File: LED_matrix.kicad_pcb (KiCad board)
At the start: 2 copper layers, 42 x 52 mm, 153 parts, among them J1 Conn_02x20_Odd_Even

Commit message: move to 0.2/0.5 vias
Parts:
- R17, R18, R19, R20, R21, R22, R23, R24, R25, R26, R27, R28, R29, R30, R31, R32: footprint Resistors_SMD:R_0603 -> Resistor_SMD:R_0603_1608Metric
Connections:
- J1 pad 1: Net-(J1-Pad1) -> (no net)
- J1 pad 10: Net-(J1-Pad10) -> (no net)
- J1 pad 11: Net-(J1-Pad11) -> (no net)
- J1 pad 12: Net-(J1-Pad12) -> (no net)
- J1 pad 13: Net-(J1-Pad13) -> (no net)
- J1 pad 14: Net-(J1-Pad14) -> (no net)
- J1 pad 17: Net-(J1-Pad17) -> (no net)
- J1 pad 2: Net-(J1-Pad2) -> (no net)
- J1 pad 20: Net-(J1-Pad20) -> (no net)
- J1 pad 24: Net-(J1-Pad24) -> (no net)
- J1 pad 25: Net-(J1-Pad25) -> (no net)
- J1 pad 26: Net-(J1-Pad26) -> (no net)
- J1 pad 27: Net-(J1-Pad27) -> (no net)
- J1 pad 28: Net-(J1-Pad28) -> (no net)
- J1 pad 3: Net-(J1-Pad3) -> (no net)
- J1 pad 30: Net-(J1-Pad30) -> (no net)
- J1 pad 34: Net-(J1-Pad34) -> (no net)
- J1 pad 39: Net-(J1-Pad39) -> (no net)
- J1 pad 4: Net-(J1-Pad4) -> (no net)
- J1 pad 5: Net-(J1-Pad5) -> (no net)
- J1 pad 6: Net-(J1-Pad6) -> (no net)
- J1 pad 7: Net-(J1-Pad7) -> (no net)
- J1 pad 8: Net-(J1-Pad8) -> (no net)
- J1 pad 9: Net-(J1-Pad9) -> (no net)
- R17 pad 2: /row_01 -> /row_0
- R18 pad 2: /row_11 -> /row_1
- R19 pad 2: /row_21 -> /row_2
- R20 pad 2: /row_31 -> /row_3
- R21 pad 2: /row_41 -> /row_4
- R22 pad 2: /row_51 -> /row_5
- R23 pad 2: /row_61 -> /row_6
- R24 pad 2: /row_71 -> /row_7
- R25 pad 2: /row_81 -> /row_8
- R26 pad 2: /row_91 -> /row_9
- R27 pad 1: /col_01 -> /col_0
- R28 pad 1: /col_11 -> /col_1
- R29 pad 1: /col_21 -> /col_2
- R30 pad 1: /col_31 -> /col_3
- R31 pad 1: /col_41 -> /col_4
- R32 pad 1: /col_51 -> /col_5
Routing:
- net /col_5: track 5.90 -> 43.7 mm, vias 0 -> 2
- net /col_4: track 8.66 -> 42.1 mm, vias 0 -> 2
- net /col_3: track 5.30 -> 35.9 mm, vias 0 -> 2
- net /row_6: track 5.62 -> 34.0 mm, vias 0 -> 2
- net /col_2: track 8.41 -> 36.3 mm, vias 0 -> 2
- net /row_7: track 8.99 -> 35.3 mm, vias 0 -> 2
- net /row_5: track 8.38 -> 33.1 mm, vias 0 -> 2
- net /col_1: track 8.28 -> 33.0 mm, vias 0 -> 2
- net /row_8: track 8.76 -> 32.8 mm, vias 0 -> 2
- net /row_4: track 6.08 -> 29.1 mm, vias 0 -> 2
- net /col_0: track 5.43 -> 27.9 mm, vias 0 -> 2
- net /row_9: track 8.98 -> 31.3 mm, vias 0 -> 2
- net /row_3: track 8.84 -> 30.9 mm, vias 0 -> 2
- net /row_2: track 5.47 -> 26.4 mm, vias 0 -> 2
- net /row_1: track 8.24 -> 28.0 mm, vias 0 -> 2
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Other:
- rule via_min_drill: 0.3 -> 0.2
- rule via_min_size: 0.6 -> 0.5

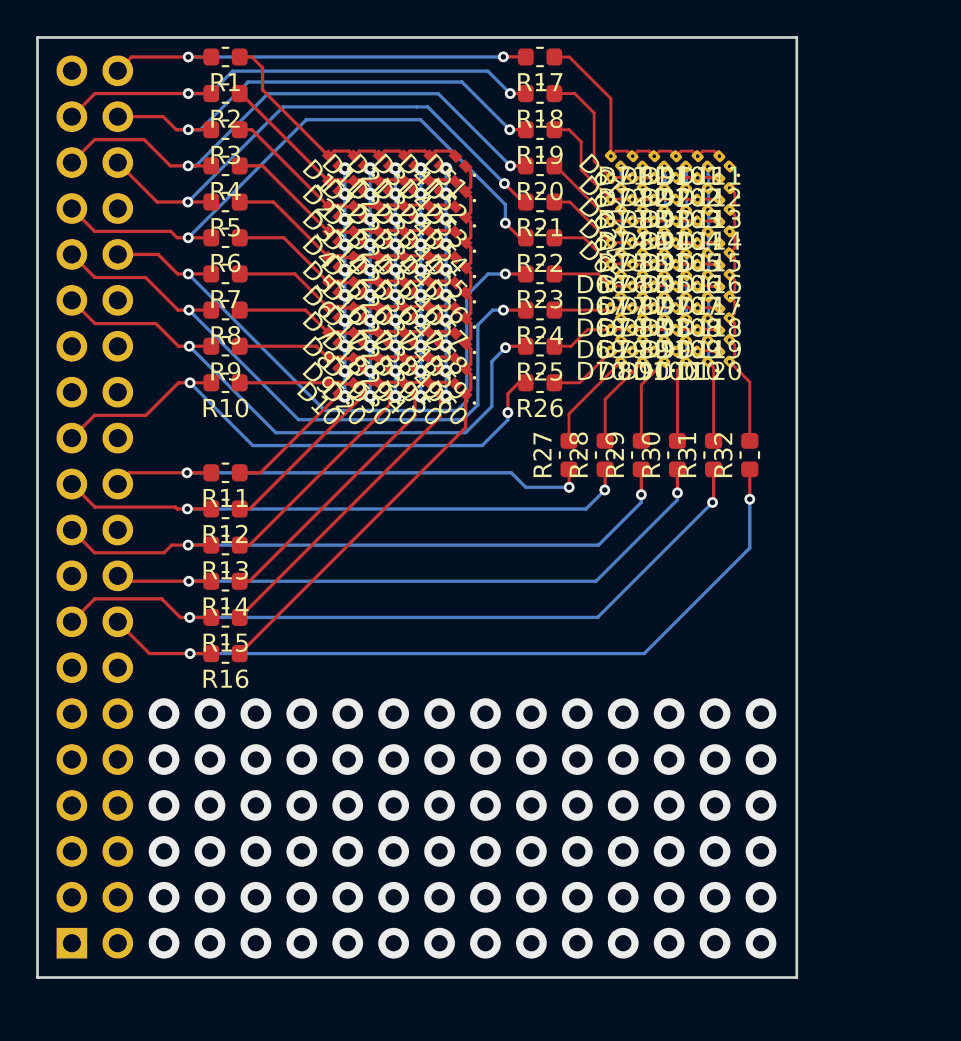
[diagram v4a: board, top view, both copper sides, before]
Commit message: generate gerber files + bugs fix
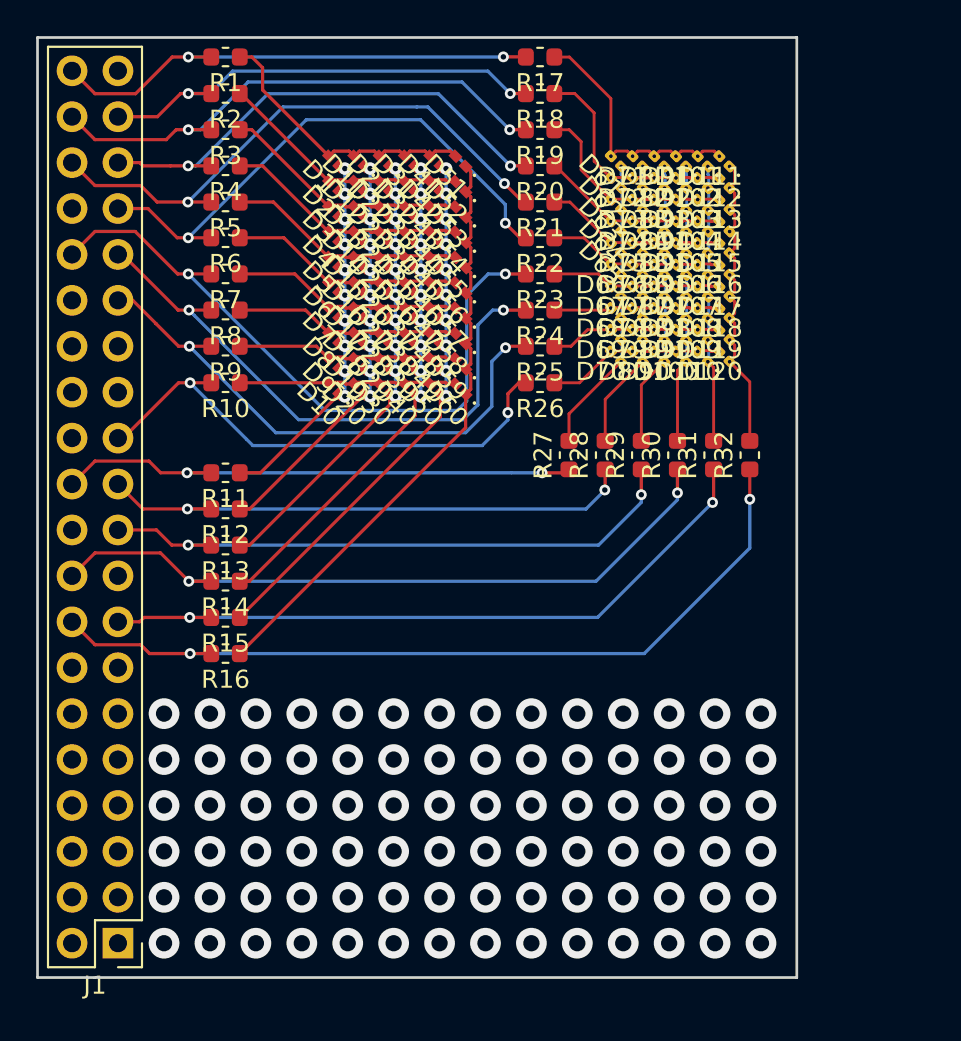
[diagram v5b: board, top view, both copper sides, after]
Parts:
- J1: moved to F.Cu
- moved J1 2.55 mm to (97.5, 131.5), turned to 180 degrees
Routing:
- net /row_3: track 30.9 -> 27.3 mm
- net /row_6: track 34.0 -> 37.6 mm
- net /row_0: track 24.2 -> 27.8 mm
- net /col_3: track 35.9 -> 39.5 mm
- net /col_4: track 42.1 -> 38.7 mm
- net /row_2: track 26.4 -> 29.4 mm
- net /col_2: track 36.3 -> 33.4 mm
- net /row_7: track 35.3 -> 32.7 mm
- net /row_5: track 33.1 -> 30.6 mm
- net /row_1: track 28.0 -> 25.4 mm
- net /row_9: track 31.3 -> 28.8 mm
- net /col_1: track 33.0 -> 30.5 mm
- net /row_8: track 32.8 -> 30.3 mm
- net /row_4: track 29.1 -> 31.7 mm
- net /col_5: track 43.7 -> 46.2 mm
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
